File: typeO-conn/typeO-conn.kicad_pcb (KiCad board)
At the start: 2 copper layers, 15.2 x 24.5 mm, 6 parts, among them J1 USB_C_Receptacle_USB2.0, J2 829-22-005-20-001101

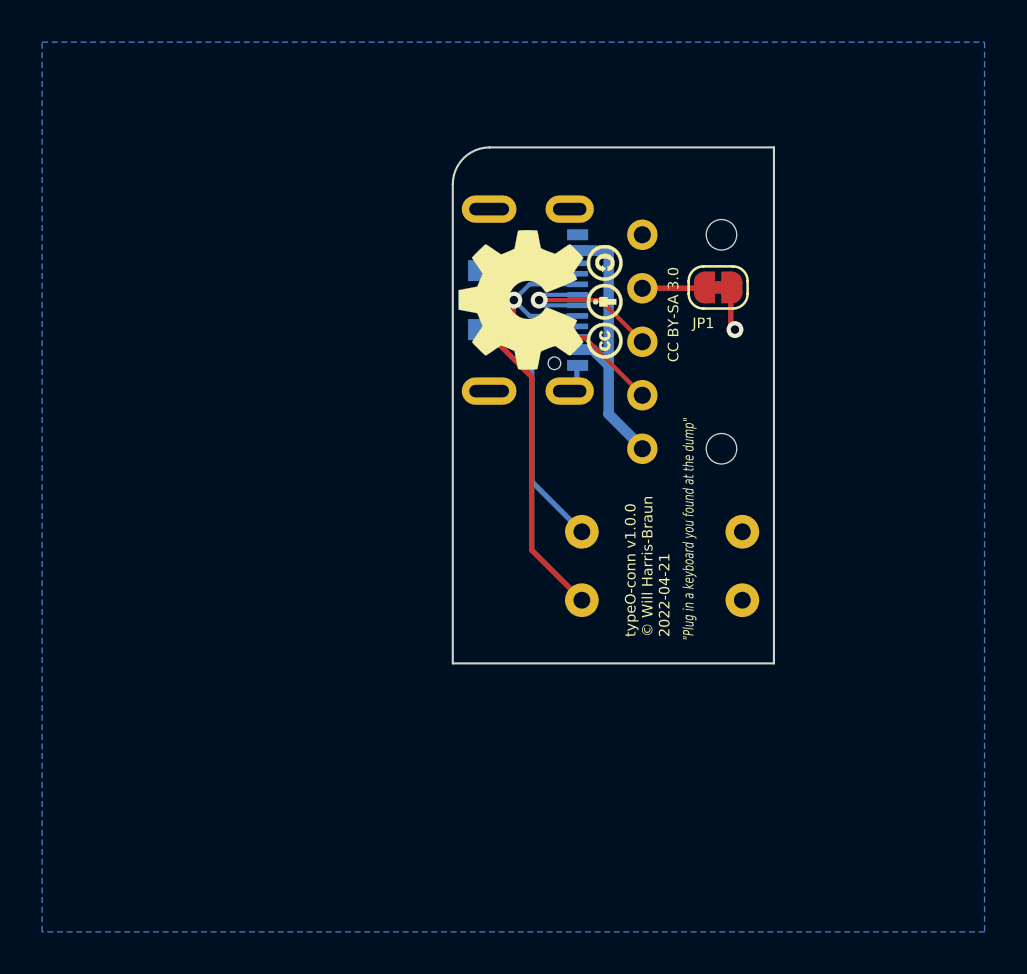
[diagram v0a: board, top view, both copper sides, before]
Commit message: Add final edge cuts
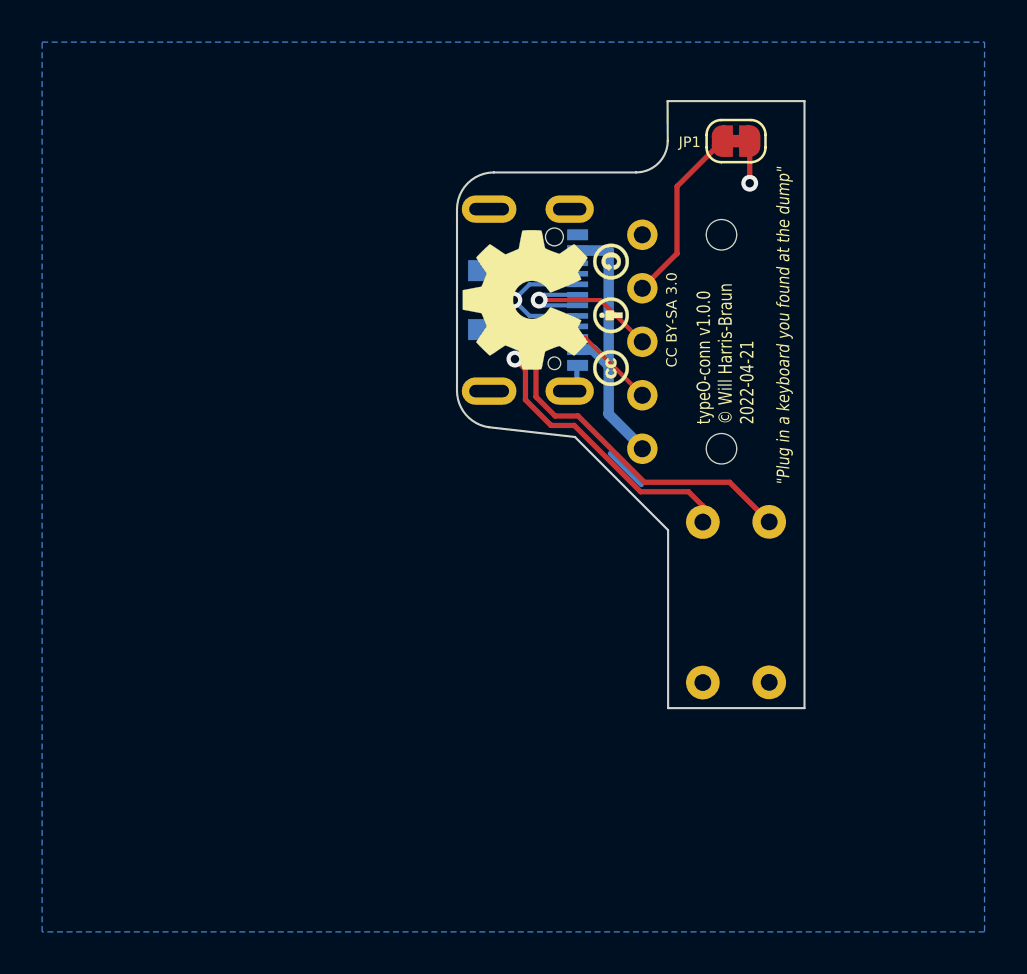
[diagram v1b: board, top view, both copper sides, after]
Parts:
- moved R2 7.40 mm to (127.1, 97.5), turned to 90 degrees
- moved JP1 7.00 mm to (128.7, 71.8)
- moved R1 4.10 mm to (130.3, 97.5), turned to 90 degrees
- moved REF** 0.20 mm to (118.7, 79.3)
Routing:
- net /ID: track 2.69 -> 8.56 mm
- net Net-(J1-PadA5): track 12.0 -> 16.8 mm, vias 0 -> 1
- net Net-(J1-PadB5): track 21.0 -> 24.0 mm
- net /GND: track 2.86 -> 4.91 mm
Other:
- board size 15.2 x 24.5 mm -> 16.5 x 28.8 mm
- board text added: "D+"
- board text added: "D-"
- board text added: "GND"
- board text added: "ID"
- board text added: "VBUS"
